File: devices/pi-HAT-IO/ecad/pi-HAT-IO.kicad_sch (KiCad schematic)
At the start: 13 parts, among them J1 GPIO, J2 5569-04A2, J3 SM04B-SRSS-TB, J4 SM04B-SRSS-TB, Q1 SI4477DY-T1-GE3, Q2 DMMT5401, U1 TLV75733PDBV

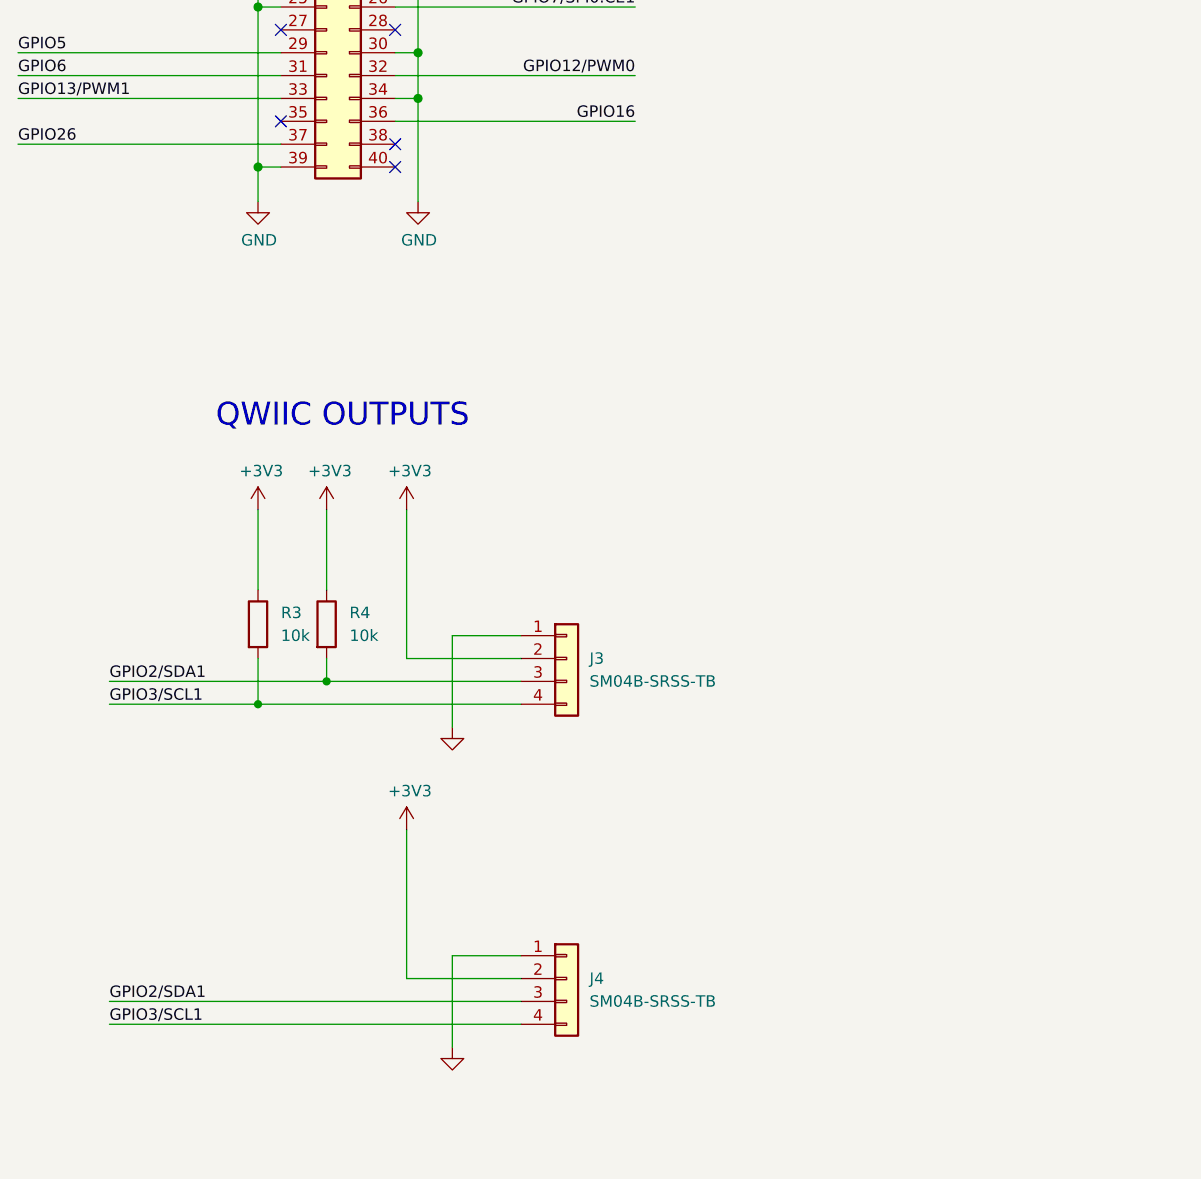
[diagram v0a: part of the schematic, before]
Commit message: Adds model for HAT header
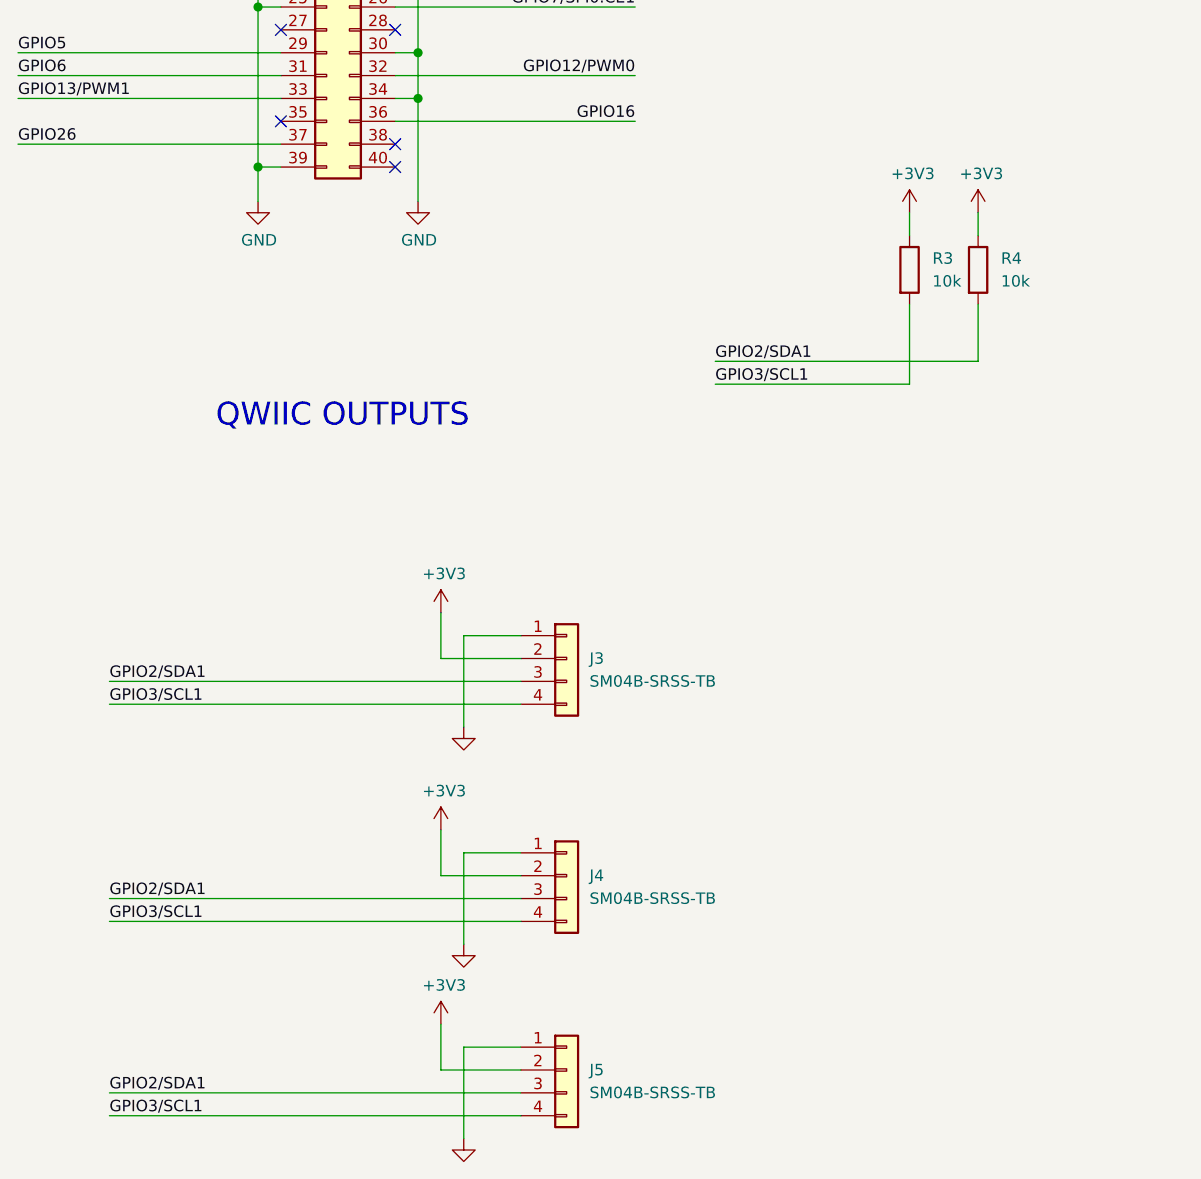
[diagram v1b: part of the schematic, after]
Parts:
- added J5: SM04B-SRSS-TB, common:JST_SH_SM04B-SRSS-TB_1x04-1MP_P1.00mm_Horizontal, symbol Connector_Generic:Conn_01x04
- J1: MPN (none) -> SPFN 16764
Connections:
- net +3V3: now also J5.2 (Pin_2)
- net GND: now also J5.1 (Pin_1)
- net GPIO2/SDA1: now also J5.3 (Pin_3)
- net GPIO3/SCL1: now also J5.4 (Pin_4)
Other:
- moved on the sheet: R3, R4

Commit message: [WIP] Reworks HAT to handle power distribution
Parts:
- added C10, C11: 100n, Capacitor_SMD:C_0603_1608Metric, symbol Device:C
- added C3, C4: 10uF, Capacitor_SMD:C_1210_3225Metric, symbol Device:C
- added C5: 100u, Capacitor_SMD:CP_Elec_10x12.6, symbol Device:C_Polarized
- added C6, C7: 47u, Capacitor_SMD:C_1210_3225Metric, symbol Device:C
- added C8: 22n, Capacitor_SMD:C_0603_1608Metric, symbol Device:C
- added C9: 330u, Capacitor_Tantalum_SMD:CP_EIA-7343-15_Kemet-W, symbol Device:C_Polarized
- added J6, J7: 47053-1000, Connector:FanPinHeader_1x04_P2.54mm_Vertical, symbol Connector_Generic:Conn_01x04
- added R10: 1.37k, Resistor_SMD:R_0603_1608Metric, symbol Device:R
- added R11, R12: 2.2k, Resistor_SMD:R_0603_1608Metric, symbol Device:R
- added R13, R14, R15, R16: 10k, Resistor_SMD:R_0805_2012Metric, symbol Device:R
- added R5: 39k, Resistor_SMD:R_0603_1608Metric, symbol Device:R
- added R6: 48.7k, Resistor_SMD:R_0603_1608Metric, symbol Device:R
- added R7: 68.1k, Resistor_SMD:R_0603_1608Metric, symbol Device:R
- added R8: 8.2k, Resistor_SMD:R_0603_1608Metric, symbol Device:R
- added R9: 10k, Resistor_SMD:R_0603_1608Metric, symbol Device:R
- added U2: PMU8418, common:PMU8000, symbol common:PMU8418
- added U3: TCA9406DC, Package_SO:SSOP-8_2.95x2.8mm_P0.65mm, symbol Interface:TCA9406DC
- R3, R4: value 10k -> 2.2k; now not fitted
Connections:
- net +3V3: now also C10.1, U3.6 (OE), U3.7 (VCCB)
- net +5V: now also Q1.1 (D), Q2.6 (E1), C6.1, C7.1, C9.1, R9.1, U2.1 (VOUT), U2.8 (VOUT); no longer J1.2 (Pin_2), J1.4 (Pin_4), Q1.3 (S), Q2.5 (E2), U1.3 (EN)
- net GND: now also C10.2, C11.2, C3.2, C4.2, C5.2, C6.2, C7.2, C9.2, J6.1 (Pin_1), J7.1 (Pin_1), R10.2, R8.2, U2.12 (PGND), U2.13 (PGND), U2.14 (PGND), U2.15 (PGND), U2.18 (PGND), U2.19 (PGND), U2.20 (PGND), U2.21 (PGND), U3.2 (GND)
- net GPIO2/SDA1: now also R12.2, U3.4 (SDA_A); no longer J3.3 (Pin_3), J4.3 (Pin_3), J5.3 (Pin_3), R4.2
- net GPIO3/SCL1: now also R11.2, U3.5 (SCL_A); no longer J3.4 (Pin_4), J4.4 (Pin_4), J5.4 (Pin_4), R3.2
- net +3V3_PI: now reaches J1.17 (Pin_17)
- net +3V3_PI: now also C11.1, R11.1, R12.1, U3.3 (VCCA)
- net VIN renamed +12V
- net +12V: now also C3.1, C4.1, C5.1, J6.2 (Pin_2), J7.2 (Pin_2), R13.1, R14.1, R15.1, R16.1, R7.1, U2.11 (VIN), U2.22 (VIN); no longer Q1.1 (D), Q2.6 (E1)
- new net +5V_PI: J1.2 (Pin_2), J1.4 (Pin_4), Q1.3 (S), Q2.5 (E2)
- new net 3V3_EN: U1.3 (EN), U2.7 (PGOOD)
- new net AGND: C8.2, R5.2, R6.2, U2.23 (AGND), U2.3 (AGND), U2.9 (AGND)
- new net EN: R7.2, R8.1, U2.10 (EN)
- new net FAN0: J6.4 (Pin_4), R14.2
- new net FAN1: J7.4 (Pin_4), R16.2
- new net FB: R10.1, R9.2, U2.2 (FB)
- new net LO: R6.1, U2.5 (LO)
- new net RT: R5.1, U2.24 (RT/CLK)
- new net SCL: J3.4 (Pin_4), J4.4 (Pin_4), J5.4 (Pin_4), R4.2, U3.8 (SCL_B)
- new net SDA: J3.3 (Pin_3), J4.3 (Pin_3), J5.3 (Pin_3), R3.2, U3.1 (SDA_B)
- new net SS: C8.1, U2.6 (SS/TR)
- new net TACHO0: J6.3 (Pin_3), R13.2
- new net TACHO1: J7.3 (Pin_3), R15.2
- no-connect marks 8 -> 7
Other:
- note added: "5V IDEAL DIODE (8 mOhm)"
- note removed: "Additional pin functions: https://pinout.xyz/"
- note removed: "VIN + IDEAL DIODE (8 mOhm)"
- moved on the sheet: C1, C2, J1, J2, J3, J4, J5, Q1, Q2A, Q2B, R1, R2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

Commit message: Reworks HAT to handle power delivery and fan control
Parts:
- added C12, C13: 100n, Capacitor_SMD:C_0603_1608Metric, symbol Device:C
- added J10: JST XH, Connector_JST:JST_XH_S2B-XH-A_1x02_P2.50mm_Horizontal, symbol Connector_Generic:Conn_01x02
- added J8, J9: JST PH, Connector_JST:JST_PH_B2B-PH-K_1x02_P2.00mm_Vertical, symbol Connector_Generic:Conn_01x02
- added Q3, Q4: DMG2305UX, Package_TO_SOT_SMD:SOT-23, symbol Device:Q_PMOS_GSD
- added R17: 10k, Resistor_SMD:R_0603_1608Metric, symbol Device:R
- added U4: EMC2302, Package_SO:MSOP-10_3x3mm_P0.5mm, symbol common:EMC2302
- added U5: MCP9804_DFN, Package_DFN_QFN:DFN-8-1EP_3x2mm_P0.5mm_EP1.7x1.4mm, symbol Sensor_Temperature:MCP9804_DFN
- J2: value 5569-04A2 -> Mini-Fit Jr; footprint common:Molex_Mini-Fit_Jr_5569-04A2_2x02_P4.20mm_Horizontal -> common:Molex_Mini-Fit_Jr_5566-04A_2x02_P4.20mm_Vertical; MPN (none) -> 39-28-8400
- J3, J4, J5: value SM04B-SRSS-TB -> JST SH; MPN (none) -> SM04B-SRSS-TB
- J6, J7: value 47053-1000 -> PC FAN HEADER; MPN (none) -> 47053-1000
- R13, R14, R15, R16: footprint Resistor_SMD:R_0805_2012Metric -> Resistor_SMD:R_0603_1608Metric; Power Rating 100mW -> (none); Tolerance 1% -> (none); now fitted
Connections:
- net +12V: now also J8.2 (Pin_2), J9.2 (Pin_2); no longer R13.1, R14.1, R15.1, R16.1
- net +3V3: now also R13.1, R14.1, C12.1, C13.1, Q4.2 (S), U4.3 (VDD), U5.8 (V_{DD}); no longer C10.1, C2.1, J3.2 (Pin_2), J4.2 (Pin_2), J5.2 (Pin_2), R3.1, R4.1, U1.5 (OUT), U3.6 (OE), U3.7 (VCCB)
- net +3V3_PI: now also R16.1, Q3.3 (D), Q4.3 (D), R17.1
- net +5V: now also J10.2 (Pin_2)
- net 3V3_EN: now also R15.1, Q3.2 (S); no longer U2.7 (PGOOD)
- net FAN0: now also U4.5 (PWM1); no longer R14.2
- net FAN1: now also U4.7 (PWM2); no longer R16.2
- net GND: now also R15.2, C12.2, C13.2, J10.1 (Pin_1), J8.1 (Pin_1), J9.1 (Pin_1), U4.4 (GND), U5.4 (GND), U5.5 (A2), U5.6 (A1), U5.7 (A0), U5.9 (EP/GND)
- net GPIO2/SDA1: now also U4.1 (SMDDATA), U5.1 (SDA)
- net GPIO3/SCL1: now also U4.2 (SMBCLK), U5.2 (SCL)
- net GPIO17 renamed GPIO17/~{3V3_OUT_EN}
- net GPIO17/~{3V3_OUT_EN}: now also Q3.1 (G), R17.2
- net GPIO27 renamed GPIO27/~{3V3_EN}
- net GPIO27/~{3V3_EN}: now also R16.2, Q4.1 (G)
- net TACHO0 renamed TACH0
- net TACH0: now also U4.6 (TACH1)
- net TACHO1 renamed TACH1
- net TACH1: now also R14.2, U4.8 (TACH2); no longer R15.2
- new net +3V3_OUT: C10.1, C2.1, J3.2 (Pin_2), J4.2 (Pin_2), J5.2 (Pin_2), R3.1, R4.1, U1.5 (OUT), U3.6 (OE), U3.7 (VCCB)
- new net 5V_GOOD: U2.7 (PGOOD)
- no-connect marks 7 -> 10
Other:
- moved on the sheet: C1, C10, C11, C2, J2, J3, J4, J5, J6, J7, Q1, Q2A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

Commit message: Standardizes BoM
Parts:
- C1, C2: MPN (none) -> CL21B105KAFNNNE; Manufacturer (none) -> Samsung Electro-Mechanics; Voltage Rating (none) -> 6.3V
- C10, C11, C12, C13: MPN (none) -> CL10B104KB8NNWC; Manufacturer (none) -> Samsung Electro-Mechanics
- C3, C4: Manufacturer (none) -> TDK Corporation
- C5: Manufacturer (none) -> Panasonic Electronic Components
- C6, C7: Manufacturer (none) -> Murata Electronics
- C8: MPN (none) -> CL10B223KB8WPNC; Manufacturer (none) -> Samsung Electro-Mechanics; Voltage Rating (none) -> 25V
- C9: Manufacturer (none) -> KEMET
- J1: MPN SPFN 16764 -> PRT-16764; Manufacturer (none) -> SparkFun
- J10, J3, J4, J5, J8, J9: Manufacturer (none) -> JST
- J2, J6, J7: Manufacturer (none) -> Molex
- Q1: Manufacturer (none) -> Vishay Siliconix
- Q2: value DMMT5401 -> DMMT5401-7-F; MPN (none) -> DMMT5401-7-F; Manufacturer (none) -> Diodes Incorporated
- Q3, Q4: MPN (none) -> DMG2305UX; Manufacturer (none) -> Diodes Incorporated
- R1, R13, R14, R15, R16, R17, R2, R9: MPN (none) -> RC0603FR-0710KL; Manufacturer (none) -> YAGEO
- R10: MPN (none) -> RC0603FR-071K37L; Manufacturer (none) -> YAGEO
- R11, R12, R3, R4: MPN (none) -> RC0603FR-072K2L; Manufacturer (none) -> YAGEO
- R5: MPN (none) -> RC0603FR-0739KL; Manufacturer (none) -> YAGEO
- R6: MPN (none) -> RC0603FR-0748K7L; Manufacturer (none) -> YAGEO
- R7: MPN (none) -> RC0603FR-0768K1L; Manufacturer (none) -> YAGEO
- R8: MPN (none) -> RC0603FR-078K2L; Manufacturer (none) -> YAGEO
- U1: MPN (none) -> TLV75733PDBV; Manufacturer (none) -> Texas Instruments
- U2: MPN (none) -> PMU8418 D; Manufacturer (none) -> Flex Power Modules
- U3: value TCA9406DC -> TCA9406DCTR; Manufacturer (none) -> Texas Instruments
- U4: Manufacturer (none) -> Microchip Technology
- U5: MPN (none) -> MCP9804T-E/MC; Manufacturer (none) -> Microchip Technology
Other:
- note added: "5V Ideal Diode (8 mOhm)"
- note added: "5V@8A Buck Converter"
- note added: "I2C Transceiver"
- note added: "On Board Temperature Sensor"
- note added: "PC Fan Controller"
- note added: "Power In/Out Connectors"
- note added: "Power Rails Controller"
- note added: "QWIIC Outputs"
- note removed: "5V IDEAL DIODE (8 mOhm)"
- note removed: "QWIIC OUTPUTS"
- moved on the sheet: C1, C10, C11, C12, C13, C2, C3, C4, C5, C6, C7, C8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

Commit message: Adds Exported BoM
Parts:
- C6, C7: MPN GRM32ER71A476K -> GRM32ER71A476KE15K
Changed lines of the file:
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@@
 			)
 		)
-		(property "MPN" "GRM32ER71A476K"
+		(property "MPN" "GRM32ER71A476KE15K"
 			(at 225.298 43.942 0)
 			(effects
@@
 			)
 		)
-		(property "MPN" "GRM32ER71A476K"
+		(property "MPN" "GRM32ER71A476KE15K"
 			(at 254.508 43.942 0)
 			(effects

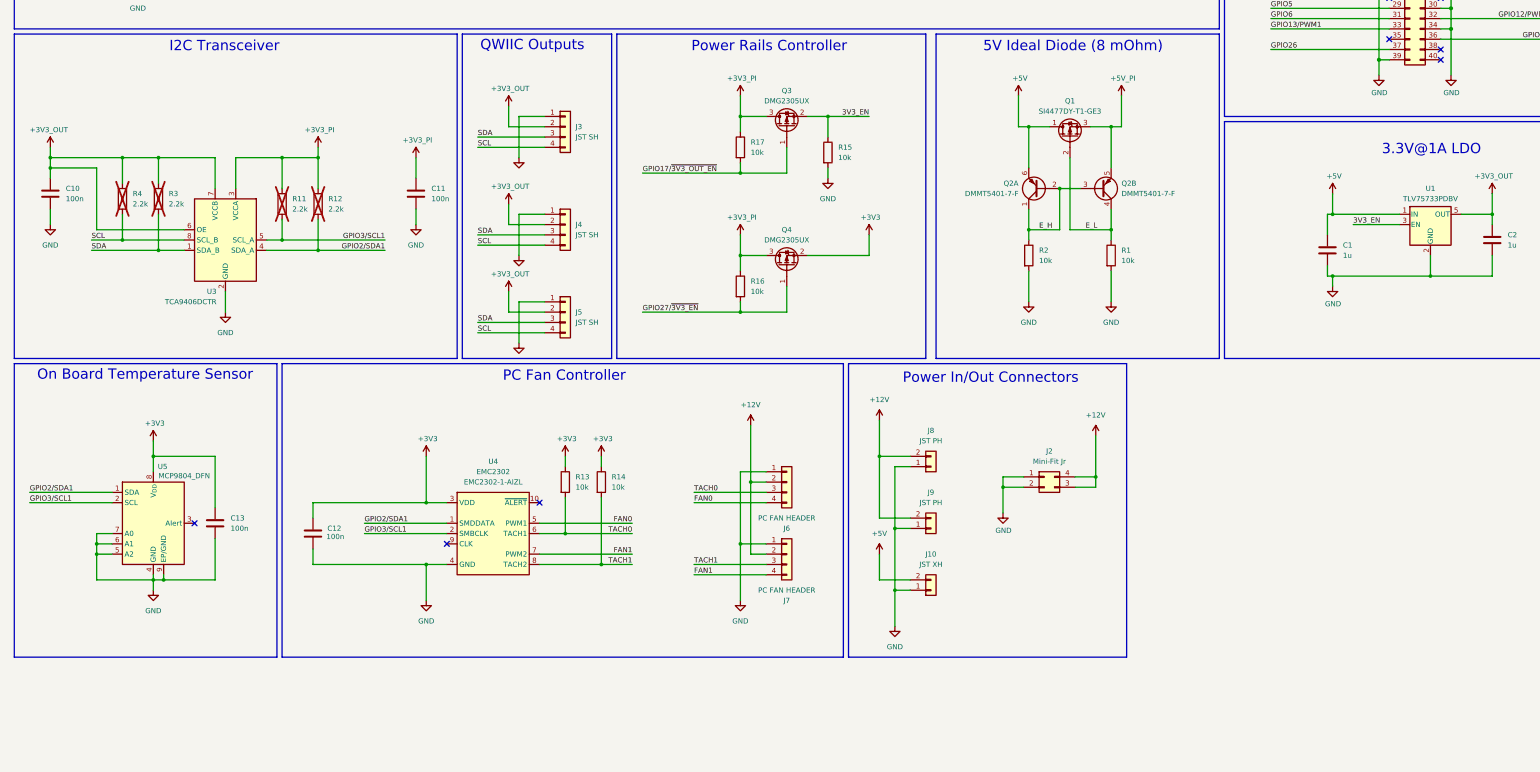
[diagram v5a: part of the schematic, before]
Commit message: Adds all datasheet for the Pi HAT
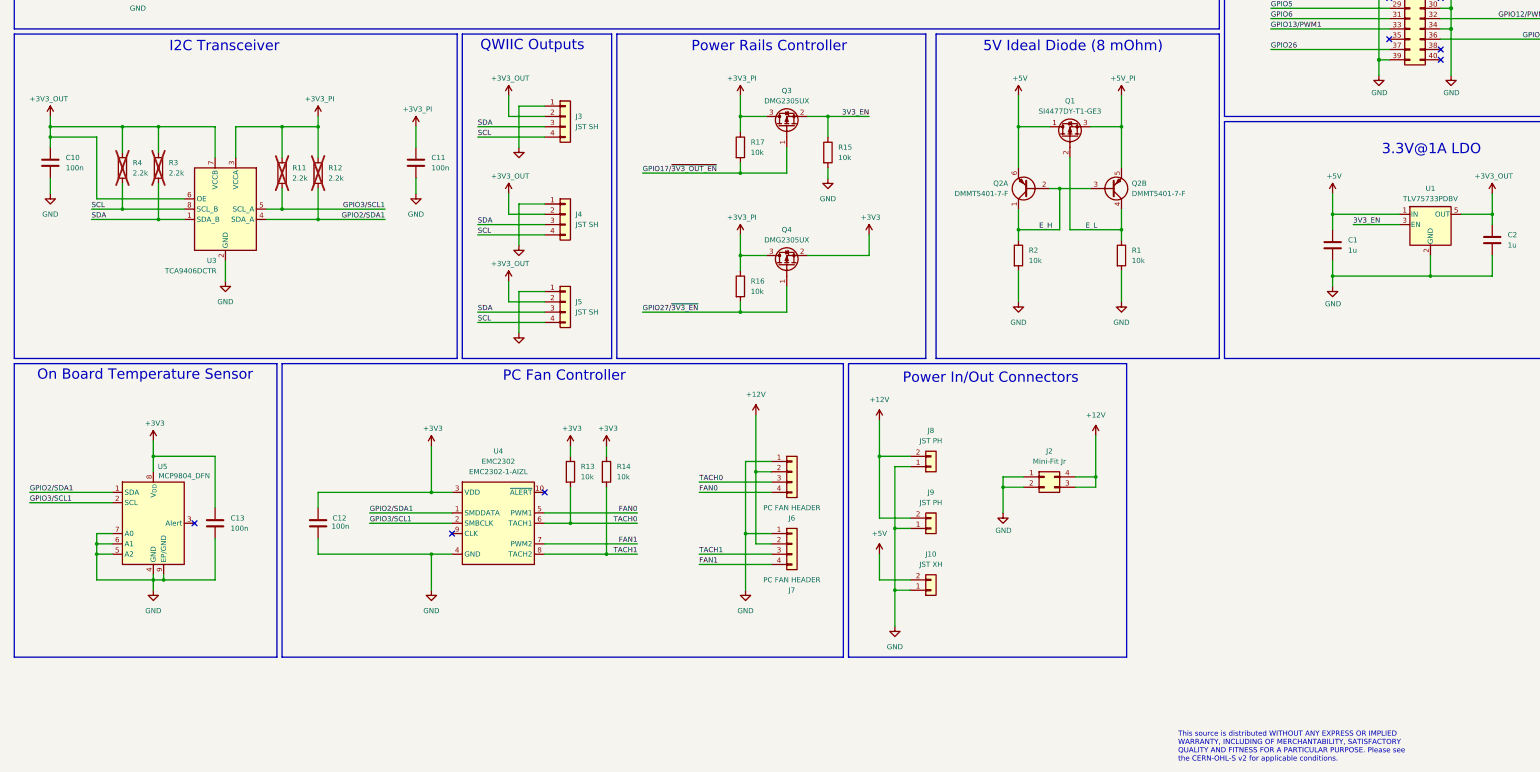
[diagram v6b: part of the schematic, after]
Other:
- note added: "This source is distributed WITHOUT ANY EXPRESS OR IMPLIED WARRANTY, INCLUDING OF MERCHANTABILITY, SATISFACTORY QUALITY AND FITNESS FOR A PARTICULAR PURPOSE. Please see the CERN-OHL-S v2 for applicable conditions."
- company: (none) -> Universitée de Lausanne
- title: (none) -> ZACI - Custom Pi HAT
- moved on the sheet: C1, C10, C11, C12, J3, J4, J5, J6, J7, Q2A, Q2B, R1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
